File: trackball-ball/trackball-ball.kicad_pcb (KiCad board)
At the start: 4 copper layers, 27.5 x 27.5 mm, 92 parts, among them J1 FH28D-28S, J2 JST-PH-3, J3 JST-PH-2, Q1 DMG6968U, U1 NRF52810-QCAA, U2 CY8CMBR3116-0x37, U3 CY8CMBR3116-0x38, U4 LTC4120-4.2, U5 BQ29700, U6 XC6206P302, Y1 32MHz-CL9pF

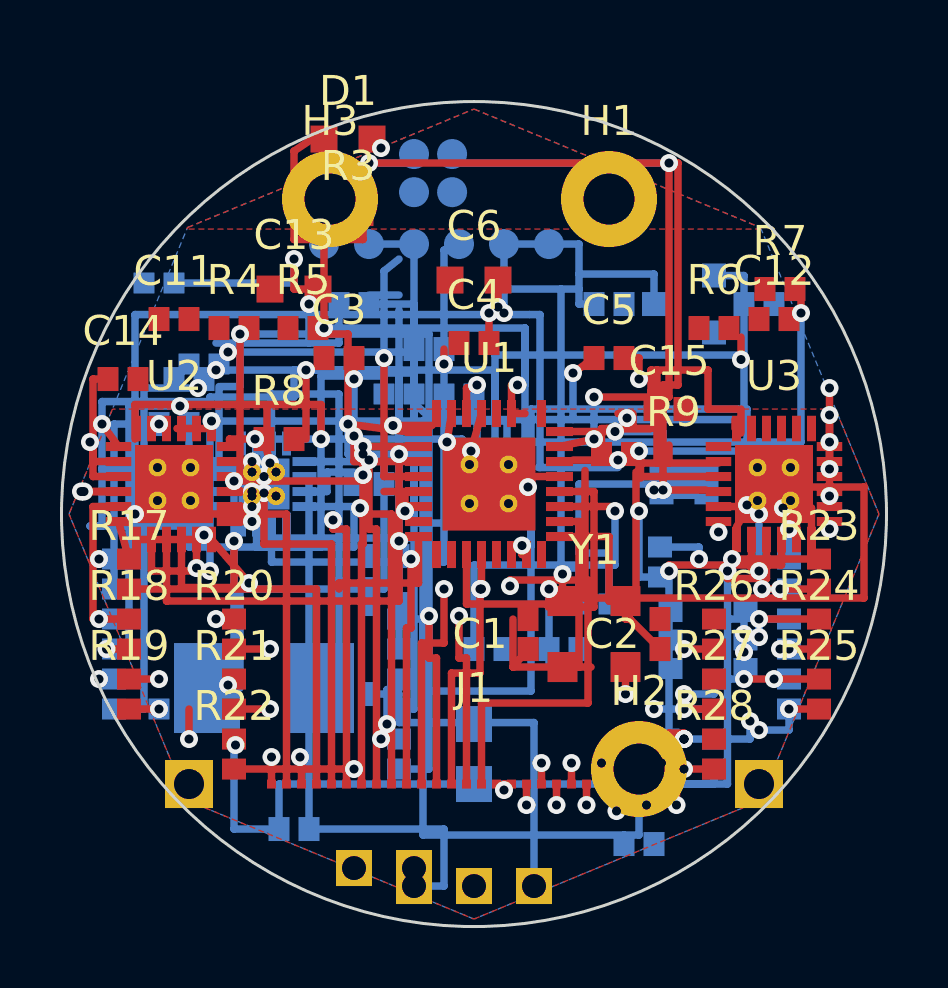
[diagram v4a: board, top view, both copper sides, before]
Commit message: ball: driver gate-7 DRC run — 21e SDA/SCL reroute triaged, 1739 violations / 87 unconnected / 92 parity (WIP, NOT clean)
Tool-run (kicad-cli 10.0.6, pcb drc --schematic-parity --severity-all + sch erc --severity-all, snapshot 2026-10-13 18:47 CDT):
- DRC: 1739 violations (+3 vs gate-6) / 87 unconnected (same) / 92 schematic parity (same)
- Shorting_items FLAT at 199 — 21e expected -3 did NOT materialize in the count; net-pair churn instead (SDA/SCL 3->1, T21/SDA 1->0, H2 NPTH-pad unnamed-net pairs up: T23 5->8, T22 0->3)
- tracks_crossing 91->95 (+4, incl new SDA ...710/...711 vs SCL ...718 B.Cu crossings); hole_to_hole 57->56 (-1, U2_CS11-via vs I2C_SCL-via ...720 pair gone)
- ERC: 510 violations (unchanged)
- (n)+(j) knot + east-field In2 census still pending; Q-C..Q-G stay PARKED
Reports: build/trackball-ball-drc-20261013-1850.json + build/trackball-ball-erc-20261013-1850.json
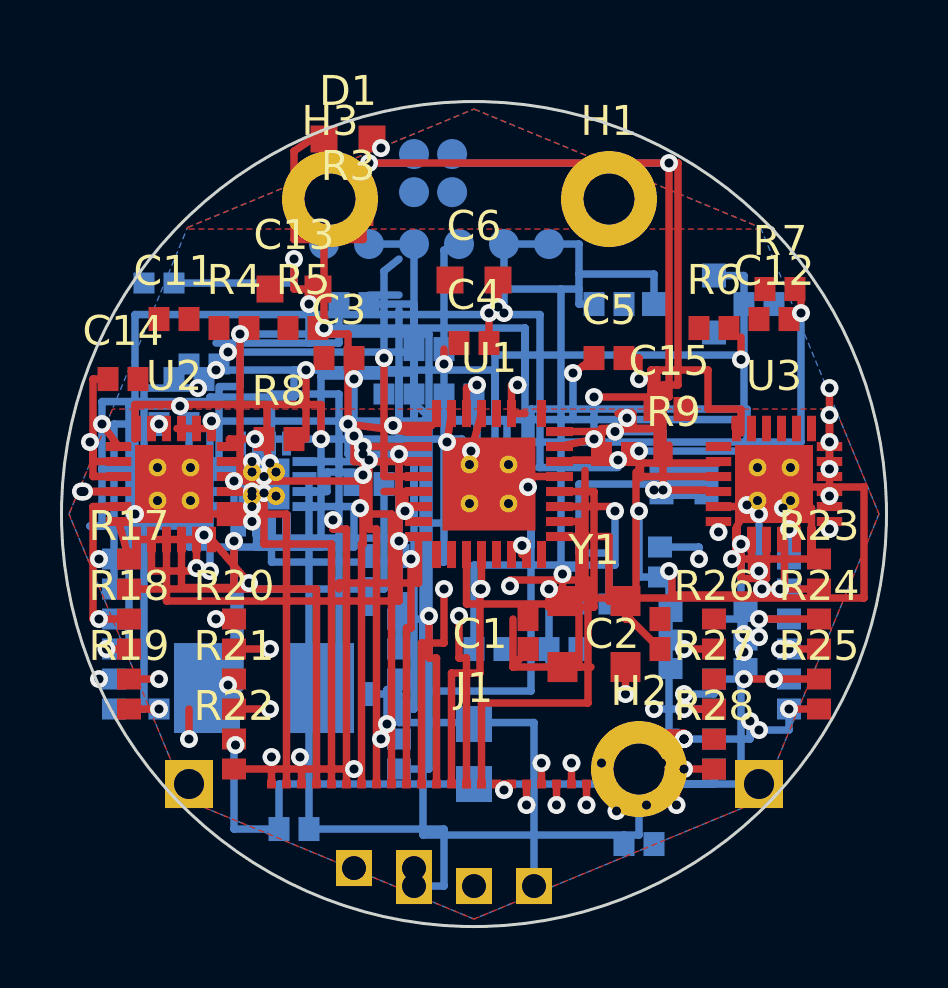
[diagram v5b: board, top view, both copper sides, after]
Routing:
- net I2C_SDA: track 55.3 -> 57.3 mm
- net I2C_SCL: track 57.6 -> 59.4 mm
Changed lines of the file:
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@@
   (segment (start 106.5 109) (end 106.5 101.9) (width 0.25) (layer "B.Cu") (net 32))
   (via (at 106.5 101.9) (size 0.6) (drill 0.3) (layers "F.Cu" "B.Cu") (net 32))
-  (segment (start 106.5 101.9) (end 106.5 101.7) (width 0.25) (layer "F.Cu") (net 32))
-  (segment (start 106.5 101.7) (end 110.25 101.7) (width 0.25) (layer "F.Cu") (net 32))
-  (segment (start 110.25 101.7) (end 110.25 101.275) (width 0.25) (layer "F.Cu") (net 32))
+  (segment (start 106.6 101.9) (end 106.6 102.7) (width 0.25) (layer "F.Cu") (net 32))
+  (segment (start 106.6 102.7) (end 110.35 102.7) (width 0.25) (layer "F.Cu") (net 32))
+  (segment (start 110.35 102.7) (end 110.35 100.9) (width 0.25) (layer "F.Cu") (net 32))
   (segment (start 105 110.7) (end 105.5 110.7) (width 0.25) (layer "B.Cu") (net 33))
   (segment (start 105.5 110.7) (end 105.5 109) (width 0.25) (layer "B.Cu") (net 33))
-  (segment (start 105.5 109) (end 108.45 109) (width 0.25) (layer "B.Cu") (net 33))
-  (segment (start 108.45 109) (end 108.45 101.9) (width 0.25) (layer "B.Cu") (net 33))
-  (via (at 108.45 101.9) (size 0.6) (drill 0.3) (layers "F.Cu" "B.Cu") (net 33))
-  (segment (start 108.45 101.9) (end 108.45 102.15) (width 0.25) (layer "F.Cu") (net 33))
-  (segment (start 108.45 102.15) (end 109.75 102.15) (width 0.25) (layer "F.Cu") (net 33))
+  (segment (start 105.5 109) (end 108.9 109) (width 0.25) (layer "B.Cu") (net 33))
+  (segment (start 108.9 109) (end 108.9 101) (width 0.25) (layer "B.Cu") (net 33))
+  (via (at 108.9 101) (size 0.6) (drill 0.3) (layers "F.Cu" "B.Cu") (net 33))
+  (segment (start 108.9 101) (end 108.9 102.15) (width 0.25) (layer "F.Cu") (net 33))
+  (segment (start 108.9 102.15) (end 109.75 102.15) (width 0.25) (layer "F.Cu") (net 33))
   (segment (start 109.75 102.15) (end 109.75 101.275) (width 0.25) (layer "F.Cu") (net 33))
   (segment (start 101.85 93.35) (end 88.7 93.35) (width 0.25) (layer "B.Cu") (net 6))
